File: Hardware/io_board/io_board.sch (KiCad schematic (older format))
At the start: 12 parts, among them J1 Conn_01x40, J2 Conn_02x05_Odd_Even, J3 Mini-DIN-6, J4 Conn_02x10_Odd_Even, U1 74LS137, U2 W65C22NxP

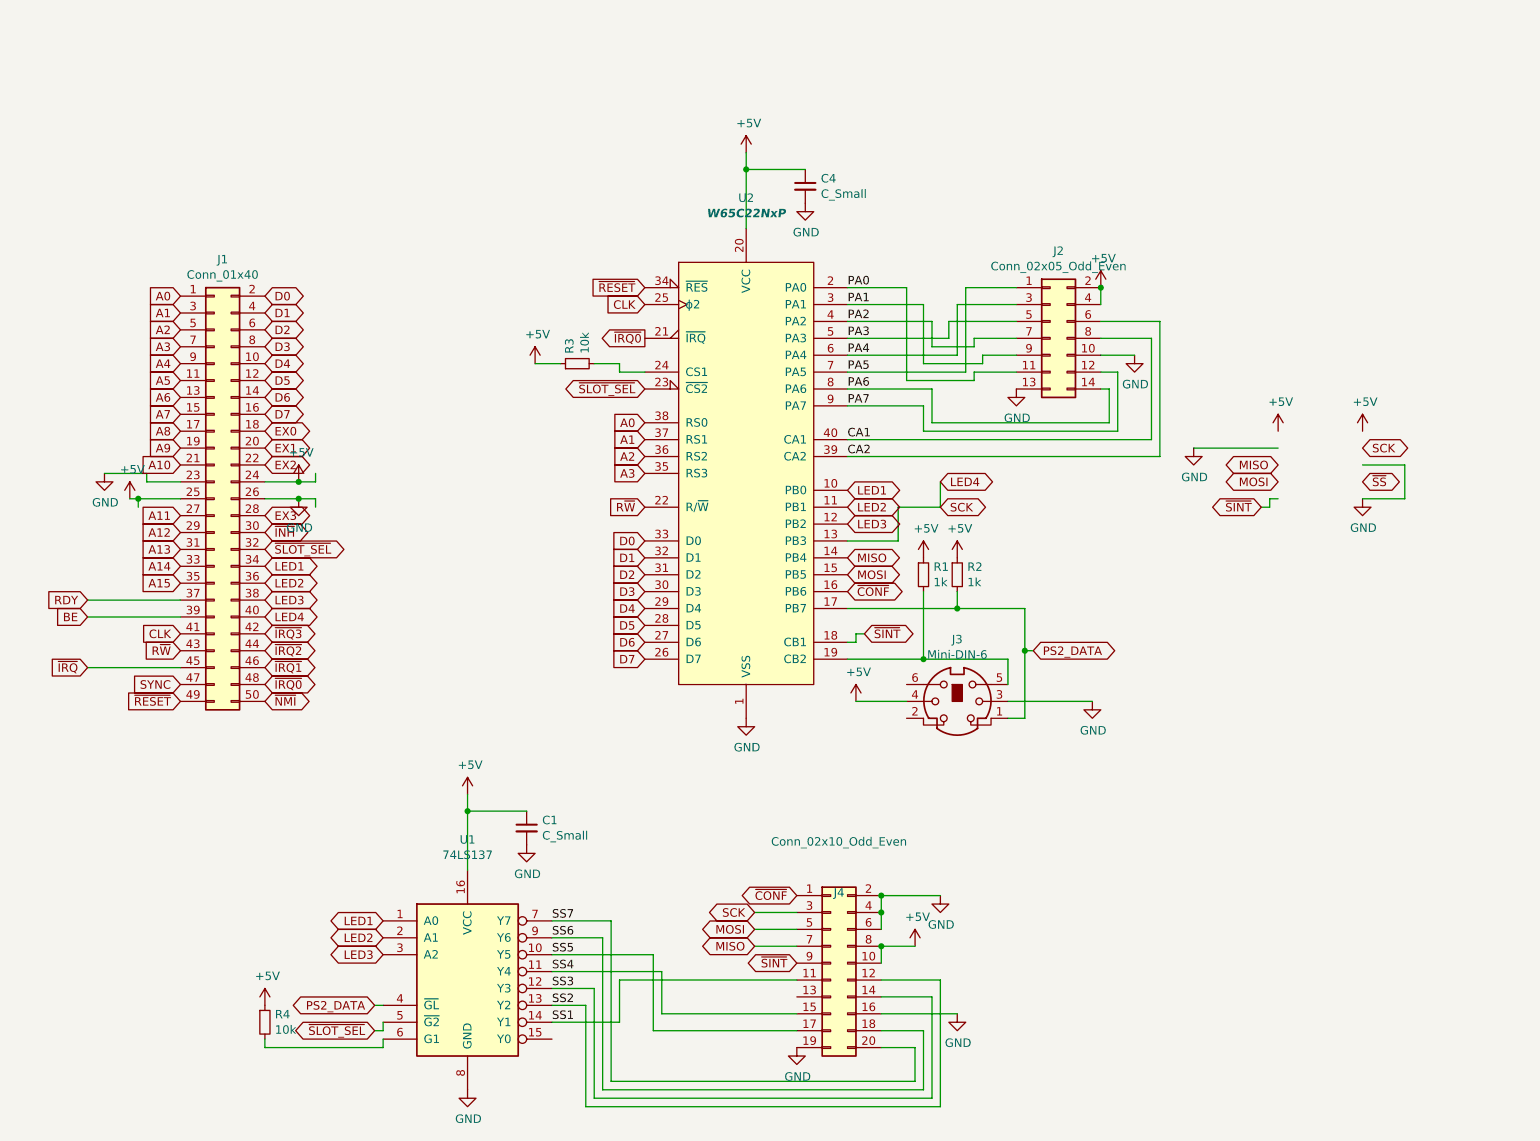
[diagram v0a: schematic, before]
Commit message: Clean up schematics and add pdfs
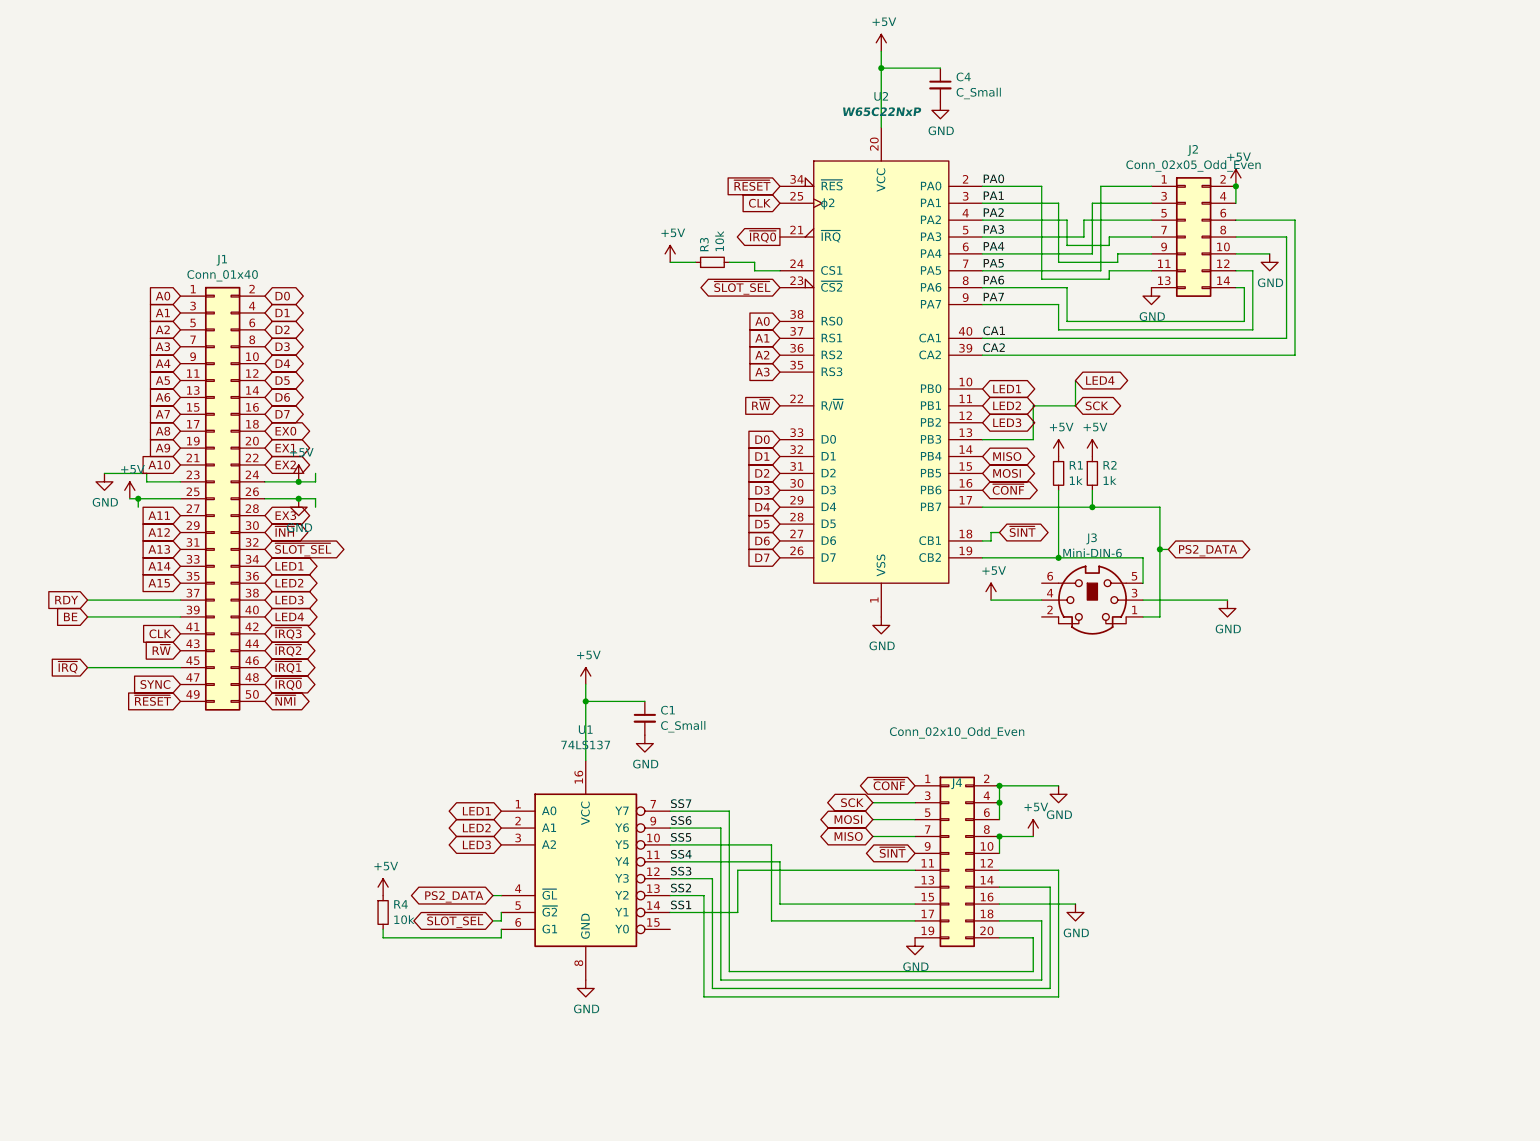
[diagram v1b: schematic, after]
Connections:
- net labels removed: ~SS~
- wire segments 138 -> 131
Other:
- moved on the sheet: C1, C4, J2, J3, J4, R1, R2, R3, R4, U1, U2

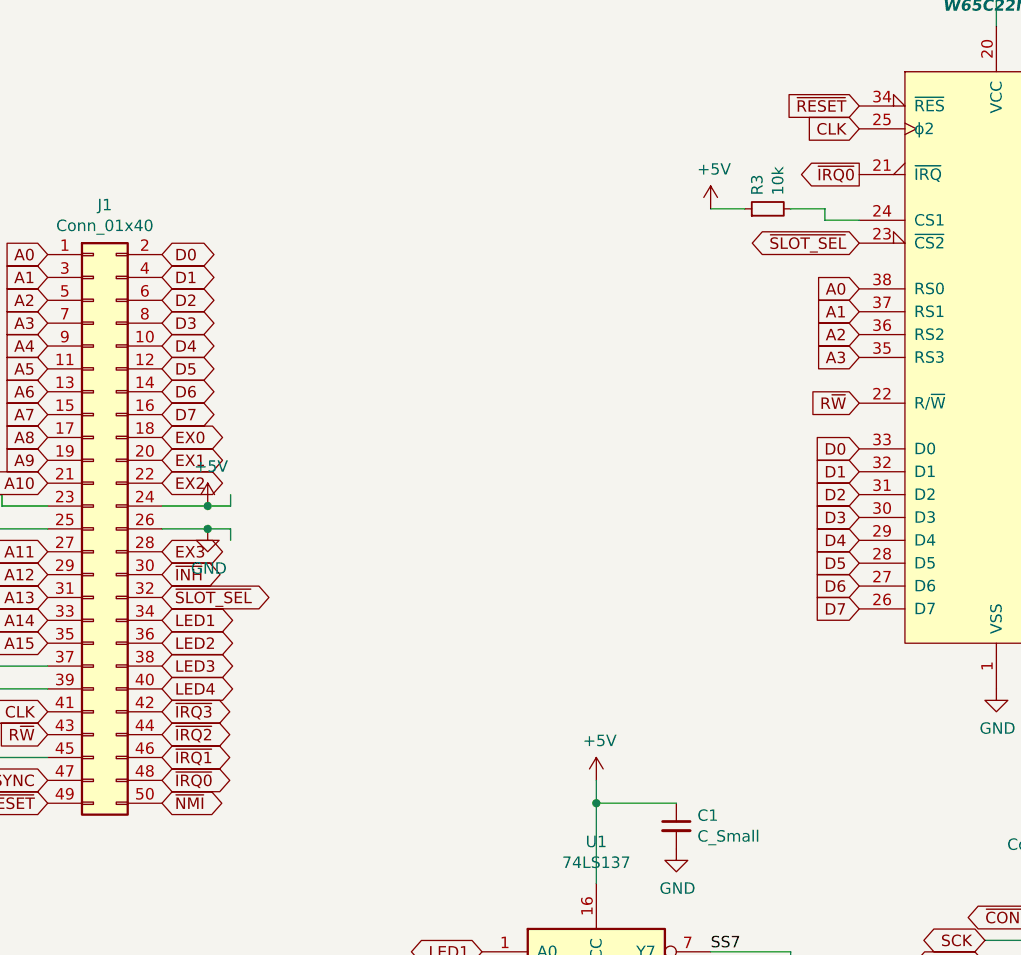
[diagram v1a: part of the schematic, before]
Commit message: Each slot has an individual interrupt line, to prevent two cards using the same interrupt line.
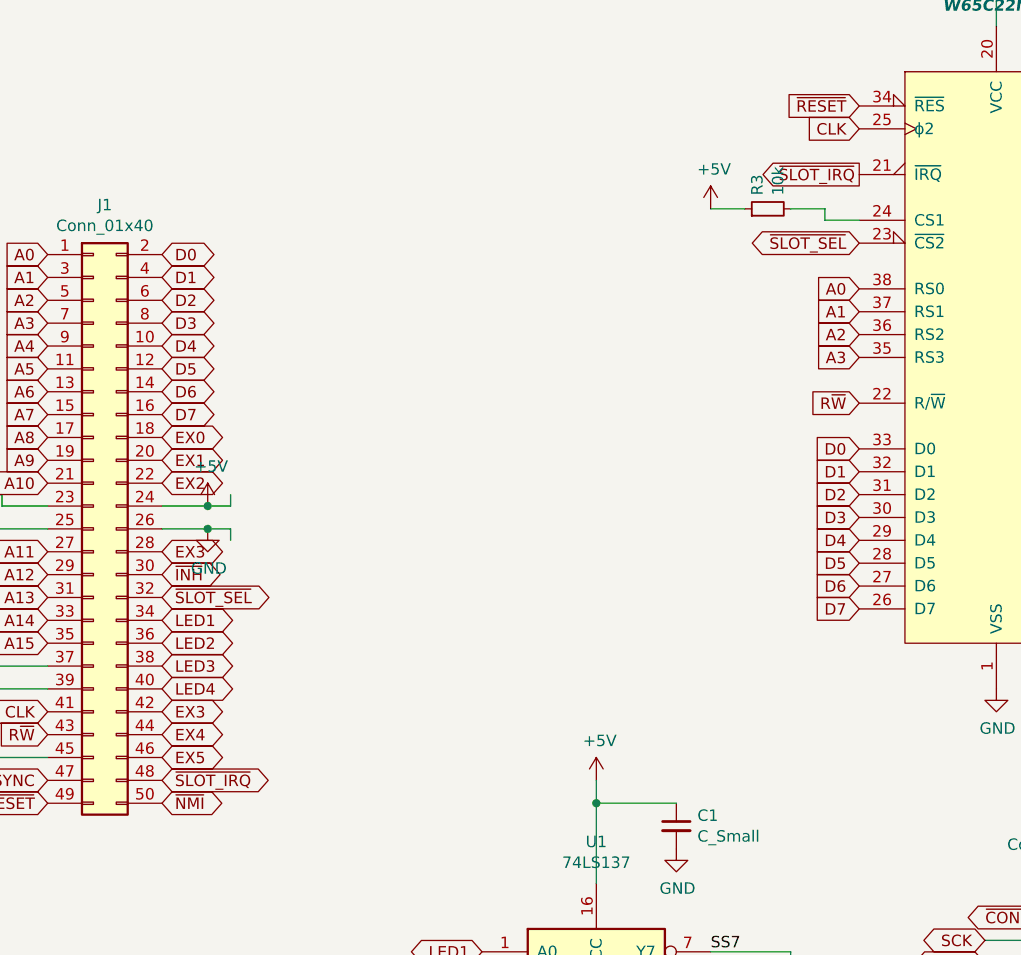
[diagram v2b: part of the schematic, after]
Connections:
- net ~IRQ3~ is gone; now on net EX3: J1.42 (Pin_42)
- net ~IRQ0~ renamed ~SLOT_IRQ~
- net ~IRQ1~ renamed EX5
- net ~IRQ2~ renamed EX4
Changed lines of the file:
@@
 ~IRQ~
 Text GLabel 2800 4550 2    50   BiDi ~ 0
-~IRQ0~
+~SLOT_IRQ~
 Text GLabel 2800 4450 2    50   BiDi ~ 0
-~IRQ1~
+EX5
 Text GLabel 2800 4350 2    50   BiDi ~ 0
-~IRQ2~
+EX4
 Text GLabel 2800 4250 2    50   BiDi ~ 0
-~IRQ3~
+EX3
 Wire Wire Line
 	3100 3300 3100 3350
@@
 ~RESET~
 Text GLabel 5850 1900 0    50   Output ~ 0
-~IRQ0~
+~SLOT_IRQ~
 Text GLabel 5850 2400 0    50   Input ~ 0
 A0
